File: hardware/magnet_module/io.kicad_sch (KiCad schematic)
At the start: 5 parts, among them J12 Conn_01x04_Pin, J13 Conn_01x02_Pin, J14 Conn_01x02_Pin

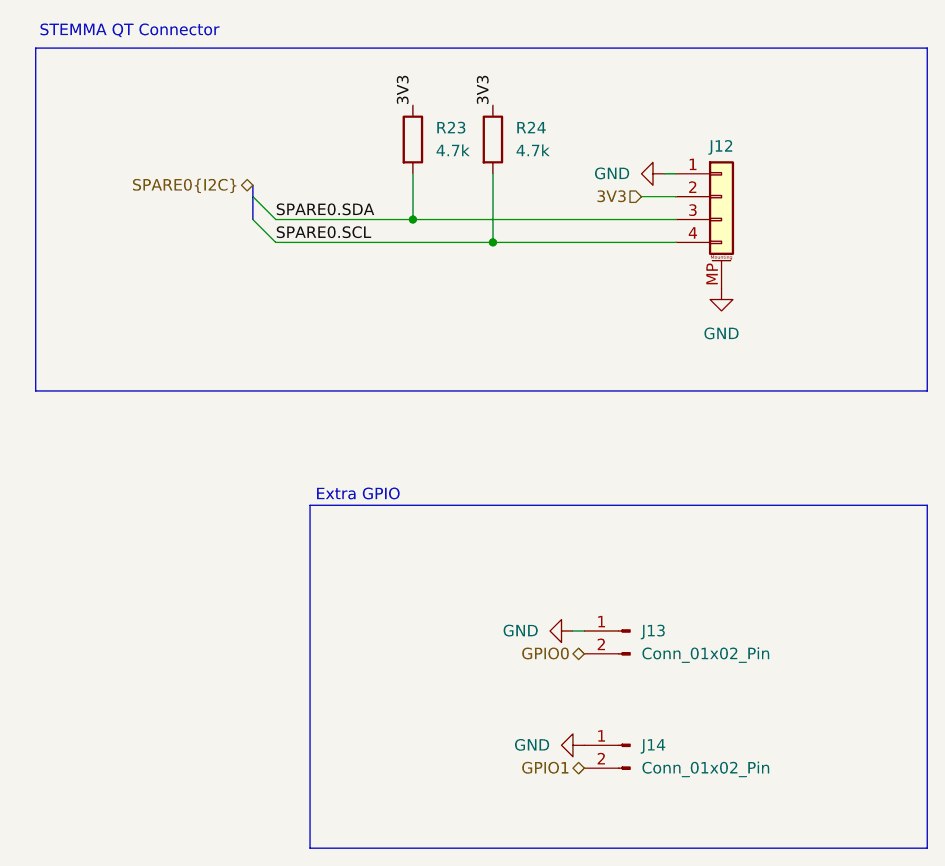
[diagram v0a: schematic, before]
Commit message: Make schematic changes for the following v1.1 changes: * Add directional & latching connector to GPIO0 & GPIO1 * Add CAN IN / CAN OUT directionality * Add pulldown to BOOT pin and pullup to nRST * Correct servo orientation
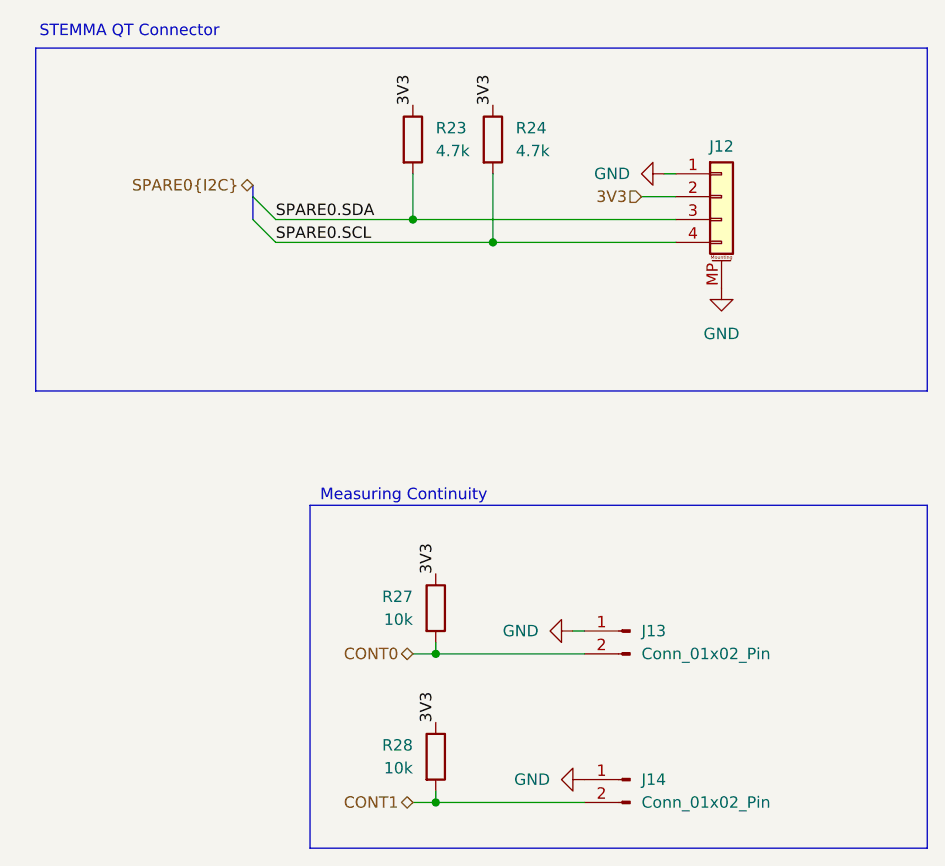
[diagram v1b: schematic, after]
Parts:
- added R27, R28: 10k, Resistor_SMD:R_0603_1608Metric, symbol Device:R
- J13, J14: LCSC C225477 -> C2938824; MPN A2541WV-2P -> 1053091102
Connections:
- net 3V3: now also R27.1, R28.1
- net GPIO0 renamed CONT0
- net CONT0: now also R27.2
- net GPIO1 renamed CONT1
- net CONT1: now also R28.2
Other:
- note added: "Measuring Continuity"
- note removed: "Extra GPIO"
- moved on the sheet: J14

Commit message: Make layout changes to support schematic changes, including assigning footprints & PNs where necessary
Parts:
- J13, J14: footprint Connector_PinHeader_2.54mm:PinHeader_1x02_P2.54mm_Vertical -> Connector_Molex:Molex_Nano-Fit_105309-xx02_1x02_P2.50mm_Vertical
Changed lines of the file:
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@@
 			)
 		)
-		(property "Footprint" "Connector_PinHeader_2.54mm:PinHeader_1x02_P2.54mm_Vertical"
+		(property "Footprint" "Connector_Molex:Molex_Nano-Fit_105309-xx02_1x02_P2.50mm_Vertical"
 			(at 137.16 102.87 0)
 			(effects
@@
 			)
 		)
-		(property "Footprint" "Connector_PinHeader_2.54mm:PinHeader_1x02_P2.54mm_Vertical"
+		(property "Footprint" "Connector_Molex:Molex_Nano-Fit_105309-xx02_1x02_P2.50mm_Vertical"
 			(at 137.16 119.38 0)
 			(effects

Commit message: Make Alogus-requested mechanical changes
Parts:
- removed J14: Conn_01x02_Pin, Connector_Molex:Molex_Nano-Fit_105309-xx02_1x02_P2.50mm_Vertical, symbol Connector:Conn_01x02_Pin
- added J11: Conn_01x02_Pin, Connector_Molex:Molex_Nano-Fit_105313-xx02_1x02_P2.50mm_Horizontal, symbol Connector:Conn_01x02_Pin
- J12: footprint Connector_JST:JST_SH_BM04B-SRSS-TB_1x04-1MP_P1.00mm_Vertical -> Connector_JST:JST_SH_SM04B-SRSS-TB_1x04-1MP_P1.00mm_Horizontal; LCSC C160390 -> C160404; MPN BM04B-SRSS-TB -> SM04B-SRSS-TB
- J13: footprint Connector_Molex:Molex_Nano-Fit_105309-xx02_1x02_P2.50mm_Vertical -> Connector_Molex:Molex_Nano-Fit_105313-xx02_1x02_P2.50mm_Horizontal; LCSC C2938824 -> C564339; MPN 1053091102 -> 1053131102
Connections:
- net CONT1: now also J11.2 (Pin_2)
- net GND: now also J11.1 (Pin_1)
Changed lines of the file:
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@@
 			)
 		)
-		(property "Footprint" "Connector_Molex:Molex_Nano-Fit_105309-xx02_1x02_P2.50mm_Vertical"
+		(property "Footprint" "Connector_Molex:Molex_Nano-Fit_105313-xx02_1x02_P2.50mm_Horizontal"
 			(at 137.16 102.87 0)
 			(effects
@@
 			)
 		)
-		(property "MPN" "1053091102"
-			(at 137.16 102.87 0)
-			(effects
-				(font
-					(size 1.27 1.27)
-				)
-				(hide yes)
-			)
-		)
-		(property "LCSC" "C2938824"
+		(property "MPN" "1053131102"
+			(at 137.16 102.87 0)
+			(effects
+				(font
+					(size 1.27 1.27)
+				)
+				(hide yes)
+			)
+		)
+		(property "LCSC" "C564339"
 			(at 137.16 102.87 0)
 			(effects
@@
 				(path "/aa5044b8-67cd-4b5a-a593-0df9431eb095/f6a6e864-0822-4ae4-be84-ceba396b8425"
 					(reference "J13")
+					(unit 1)
+				)
+			)
+		)
+	)
+	(symbol
+		(lib_id "Connector:Conn_01x02_Pin")
+		(at 137.16 119.38 0)
+		(mirror y)
+		(unit 1)
+		(exclude_from_sim no)
+		(in_bom yes)
+		(on_board yes)
+		(dnp no)
+		(fields_autoplaced yes)
+		(property "Reference" "J11"
+			(at 138.43 119.3799 0)
+			(effects
+				(font
+					(size 1.27 1.27)
+				)
+				(justify right)
+			)
+		)
+		(property "Value" "Conn_01x02_Pin"
+			(at 138.43 121.9199 0)
+			(effects
+				(font
+					(size 1.27 1.27)
+				)
+				(justify right)
+			)
+		)
+		(property "Footprint" "Connector_Molex:Molex_Nano-Fit_105313-xx02_1x02_P2.50mm_Horizontal"
+			(at 137.16 119.38 0)
+			(effects
+				(font
+					(size 1.27 1.27)
+				)
+				(hide yes)
+			)
+		)
+		(property "Datasheet" "~"
+			(at 137.16 119.38 0)
+			(effects
+				(font
+					(size 1.27 1.27)
+				)
+				(hide yes)
+			)
+		)
+		(property "Description" "Generic connector, single row, 01x02, script generated"
+			(at 137.16 119.38 0)
+			(effects
+				(font
+					(size 1.27 1.27)
+				)
+				(hide yes)
+			)
+		)
+		(property "MPN" "1053131102"
+			(at 137.16 119.38 0)
+			(effects
+				(font
+					(size 1.27 1.27)
+				)
+				(hide yes)
+			)
+		)
+		(property "LCSC" "C564339"
+			(at 137.16 119.38 0)
+			(effects
+				(font
+					(size 1.27 1.27)
+				)
+				(hide yes)
+			)
+		)
+		(pin "1"
+		)
+		(pin "2"
+		)
+		(instances
+			(project "magnet"
+				(path "/aa5044b8-67cd-4b5a-a593-0df9431eb095/f6a6e864-0822-4ae4-be84-ceba396b8425"
+					(reference "J11")
 					(unit 1)
 				)
@@
 			)
 		)
-		(property "Footprint" "Connector_JST:JST_SH_BM04B-SRSS-TB_1x04-1MP_P1.00mm_Vertical"
+		(property "Footprint" "Connector_JST:JST_SH_SM04B-SRSS-TB_1x04-1MP_P1.00mm_Horizontal"
 			(at 147.32 54.61 0)
 			(effects
@@
 			)
 		)
-		(property "MPN" "BM04B-SRSS-TB"
-			(at 147.32 54.61 0)
-			(effects
-				(font
-					(size 1.27 1.27)
-				)
-				(hide yes)
-			)
-		)
-		(property "LCSC" "C160390"
+		(property "MPN" "SM04B-SRSS-TB"
+			(at 147.32 54.61 0)
+			(effects
+				(font
+					(size 1.27 1.27)
+				)
+				(hide yes)
+			)
+		)
+		(property "LCSC" "C160404"
 			(at 147.32 54.61 0)
 			(effects
@@
 					(unit 1)
 				)
-			)
-		)
-	)
-	(symbol
-		(lib_id "Connector:Conn_01x02_Pin")
-		(at 137.16 119.38 0)
-		(mirror y)
-		(unit 1)
-		(exclude_from_sim no)
-		(in_bom yes)
-		(on_board yes)
-		(dnp no)
-		(fields_autoplaced yes)
-		(property "Reference" "J14"
-			(at 138.43 119.3799 0)
-			(effects
-				(font
-					(size 1.27 1.27)
-				)
-				(justify right)
-			)
-		)
-		(property "Value" "Conn_01x02_Pin"
-			(at 138.43 121.9199 0)
-			(effects
-				(font
-					(size 1.27 1.27)
-				)
-				(justify right)
-			)
-		)
-		(property "Footprint" "Connector_Molex:Molex_Nano-Fit_105309-xx02_1x02_P2.50mm_Vertical"
-			(at 137.16 119.38 0)
-			(effects
-				(font
-					(size 1.27 1.27)
-				)
-				(hide yes)
-			)
-		)
-		(property "Datasheet" "~"
-			(at 137.16 119.38 0)
-			(effects
-				(font
-					(size 1.27 1.27)
-				)
-				(hide yes)
-			)
-		)
-		(property "Description" "Generic connector, single row, 01x02, script generated"
-			(at 137.16 119.38 0)
-			(effects
-				(font
-					(size 1.27 1.27)
-				)
-				(hide yes)
-			)
-		)
-		(property "MPN" "1053091102"
-			(at 137.16 119.38 0)
-			(effects
-				(font
-					(size 1.27 1.27)
-				)
-				(hide yes)
-			)
-		)
-		(property "LCSC" "C2938824"
-			(at 137.16 119.38 0)
-			(effects
-				(font
-					(size 1.27 1.27)
-				)
-				(hide yes)
-			)
-		)
-		(pin "1"
-		)
-		(pin "2"
-		)
-		(instances
-			(project "magnet"
-				(path "/aa5044b8-67cd-4b5a-a593-0df9431eb095/f6a6e864-0822-4ae4-be84-ceba396b8425"
-					(reference "J14")
-					(unit 1)
-				)

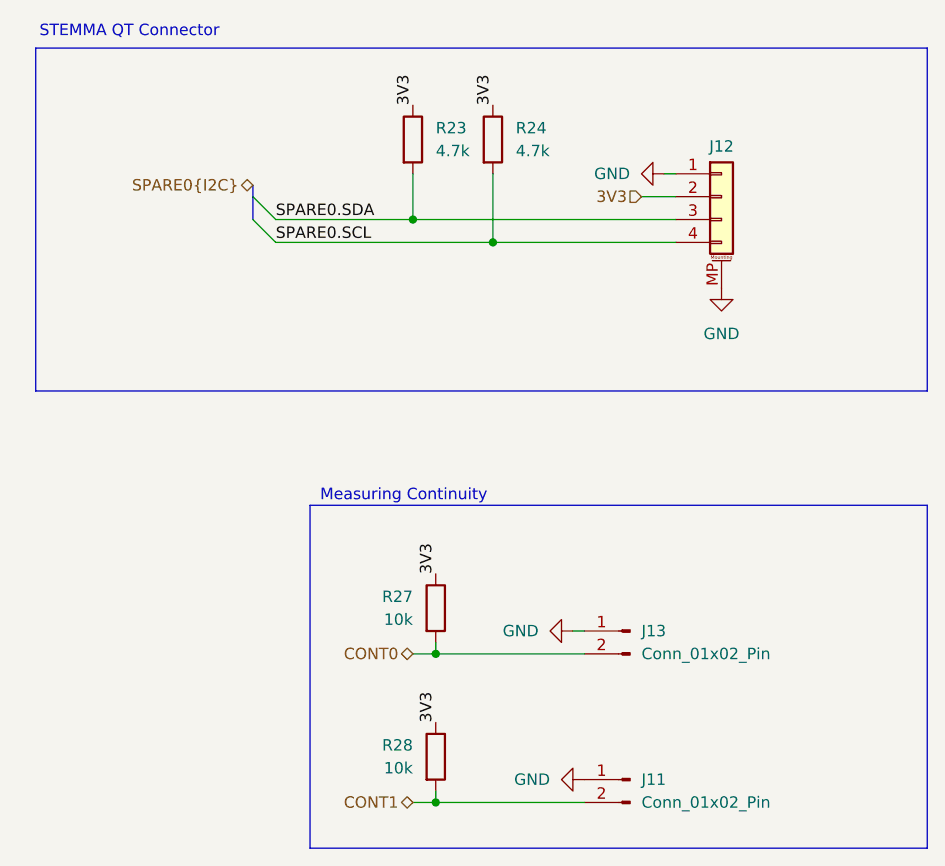
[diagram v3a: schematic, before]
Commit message: add test points to schematic, generate step file including ultrasonic mic
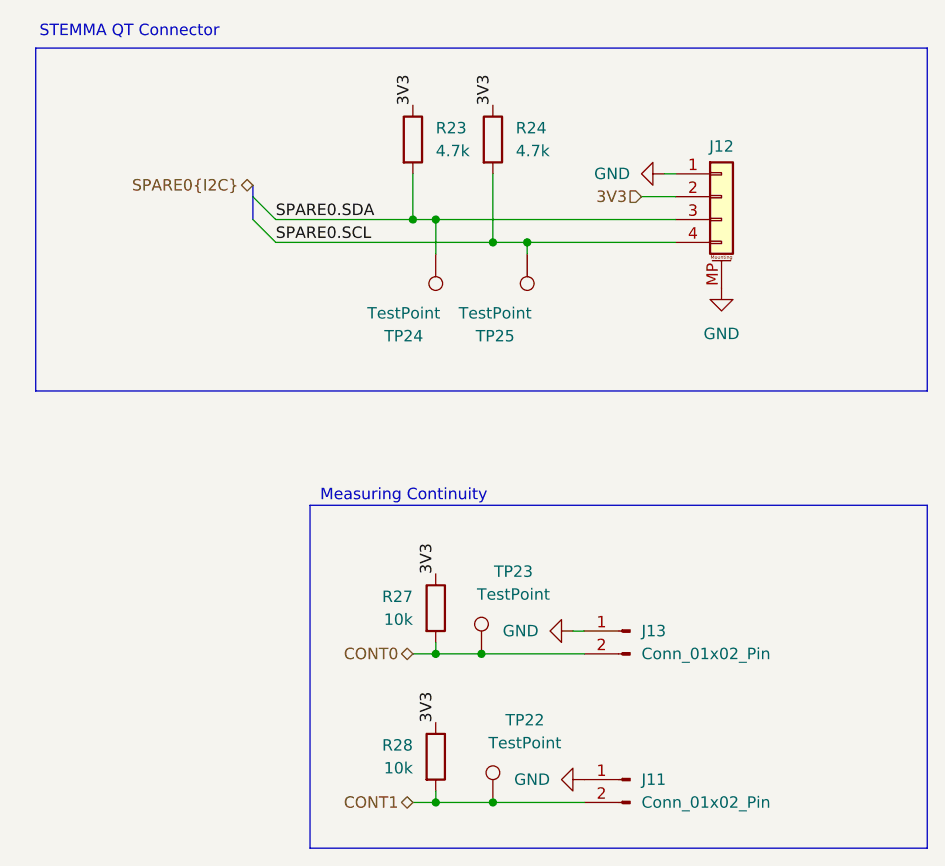
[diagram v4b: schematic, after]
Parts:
- added TP22, TP23, TP24, TP25: TestPoint, TestPoint:TestPoint_Pad_1.0x1.0mm, symbol Connector:TestPoint
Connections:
- net CONT0: now also TP23.1
- net CONT1: now also TP22.1
- net SPARE0.SCL: now also TP25.1
- net SPARE0.SDA: now also TP24.1
